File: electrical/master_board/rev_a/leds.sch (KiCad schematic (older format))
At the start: 50 parts, among them Q10 2N7000;SOT23, Q11 2N7000;SOT23, Q12 2N7000;SOT23, Q13 2N7000;SOT23, Q14 2N7000;SOT23, Q15 2N7000;SOT23, Q16 2N7000;SOT23, Q20 2N7000;SOT23, Q21 2N7000;SOT23, Q22 2N7000;SOT23, Q23 2N7000;SOT23, Q24 2N7000;SOT23, Q25 2N7000;SOT23, Q7 2N7000;SOT23, Q8 2N7000;SOT23, Q9 2N7000;SOT23, U5 SN74HCS595;TTSOP16, U8 SN74HCS595;TTSOP16

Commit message: Cleaned up schematics some.
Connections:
- net labels added: LED8_TO_LED9, LED_SCK, ~LED_NSS, ~NRST
- wire segments 187 -> 183
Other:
- moved on the sheet: U5, U8

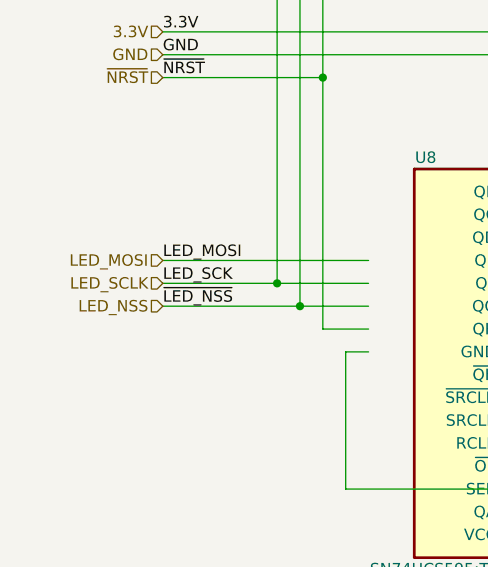
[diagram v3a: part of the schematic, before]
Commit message: Bound signals to Morpho pins.
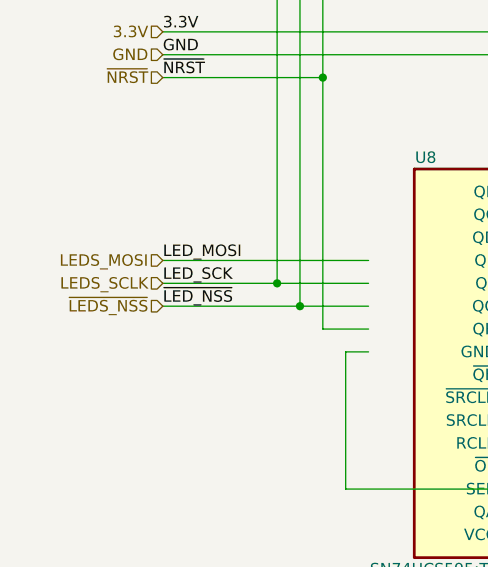
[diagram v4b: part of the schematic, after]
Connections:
- net labels added: LEDS_MOSI, LEDS_SCLK, ~LEDS_NSS
- net labels removed: LED_NSS, LED_SCLK
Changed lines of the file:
@@
 $Descr A4 11693 8268
 encoding utf-8
-Sheet 4 10
+Sheet 10 10
 Title "HR2 LED's"
 Date "2020-10-17"
@@
 	9700 3200 9700 2300
 Text HLabel 1000 5400 0    50   Input ~ 0
-LED_MOSI
+LEDS_MOSI
 Text HLabel 1000 5500 0    50   Input ~ 0
-LED_SCLK
+LEDS_SCLK
 $Comp
 L HR2:SN74HCS595;TTSOP16 U?
@@
 	3000 2700 6500 2700
 Text HLabel 1000 5600 0    50   Input ~ 0
-LED_NSS
+~LEDS_NSS
 Wire Bus Line
 	3500 2000 3500 6100

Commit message: Schematic is basically complete.
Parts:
- added C24, C25: 10pF;1608, symbol Device:C
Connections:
- wire segments 183 -> 189
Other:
- note added: "ByPass Capacitors"
- note added: "Power\nBus"
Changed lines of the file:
@@
 $Descr A4 11693 8268
 encoding utf-8
-Sheet 10 10
+Sheet 7 10
 Title "HR2 LED's"
 Date "2020-10-17"
@@
 Comment4 ""
 $EndDescr
-Text Notes 1050 1950 0    50   ~ 0
+Text Notes 900  1900 0    50   ~ 0
 Note:\n1. The LED's are controlled by a 16-bit shift regester that is\n   filled using an SPI controller.  The 3.3V outputs are fed into\n   FET's that drive the LED's.\n
-Connection ~ 4500 6400
-Wire Wire Line
-	4500 6400 3100 6400
 Wire Wire Line
 	9300 4200 10100 4200
@@
 AR Path="/5FA4A874/5FB58AAF" Ref="U8"  Part="1"
 F 0 "U8" H 2150 5250 50  0000 C CNN
-F 1 "SN74HCS595;TTSOP16" H 2300 3450 50  0000 C CNN
+F 1 "SN74HCS595;TTSOP16" H 2450 3950 50  0000 C CNN
 F 2 "Package_SO:TSSOP-16_4.4x5mm_P0.65mm" H 2100 5150 60  0001 L CNN
 F 3 "Tri-state 8-Bit Shift Register" H 2100 4950 60  0001 L CNN
@@
 Text Label 3400 5700 2    50   ~ 0
 LED6
-Text Notes 2250 1500 0    50   ~ 0
+Text Notes 1850 2000 0    50   ~ 0
 16-Bit SPI LED Shift Register
 Wire Wire Line
@@
 Text HLabel 1000 4500 0    50   Input ~ 0
 GND
-Wire Wire Line
-	10100 6400 10900 6400
-Wire Wire Line
-	10900 6400 10900 3500
-Wire Wire Line
-	10900 3500 10100 3500
-Connection ~ 10100 6400
-Connection ~ 10100 3500
-Wire Wire Line
-	4500 4200 3700 4200
-Wire Wire Line
-	3700 4200 3700 1300
-Wire Wire Line
-	3700 1300 4500 1300
 Connection ~ 4500 4200
 Text HLabel 1000 1300 0    50   Input ~ 0
@@
 Text HLabel 1000 4400 0    50   Input ~ 0
 3.3V
-Connection ~ 3700 1300
-Wire Wire Line
-	1000 1300 3700 1300
 Wire Wire Line
 	3000 5200 9700 5200
@@
 	3400 5100 3500 5000
 Entry Wire Line
-	3400 6100 3500 6000
+	3400 6400 3500 6300
 Wire Wire Line
 	3000 5100 3400 5100
 Wire Wire Line
-	3400 6100 3100 6100
+	3400 6400 3100 6400
 Wire Wire Line
 	1900 5800 1800 5800
@@
 Wire Wire Line
 	3100 6400 3100 6100
-Connection ~ 3100 6100
 Wire Wire Line
 	3100 6100 3000 6100
-Connection ~ 3100 6400
 Wire Wire Line
 	1800 6400 3100 6400
@@
 Text Label 3400 5100 2    50   ~ 0
 3.3V
-Text Label 3400 6100 2    50   ~ 0
+Text Label 3400 6400 2    50   ~ 0
 GND
 NoConn ~ 3000 6000
@@
 Text HLabel 1000 5600 0    50   Input ~ 0
 ~LEDS_NSS
+Text Notes 3250 3950 0    50   ~ 0
+Power\nBus
+Entry Wire Line
+	3600 3500 3500 3400
+Text Label 3600 3500 0    50   ~ 0
+GND
+Wire Wire Line
+	3600 3500 4500 3500
+Connection ~ 4500 3500
+Connection ~ 3100 6400
+Entry Wire Line
+	3600 6400 3500 6300
+Wire Wire Line
+	3600 6400 4500 6400
+Connection ~ 4500 6400
+Text Label 3600 6400 0    50   ~ 0
+GND
+Entry Wire Line
+	3500 1400 3400 1300
+Entry Wire Line
+	3500 1400 3600 1300
+Entry Wire Line
+	3950 1000 4050 1100
+Wire Wire Line
+	1000 1300 3400 1300
+Text Label 3400 1300 2    50   ~ 0
+P5V
+Text Label 3600 1300 0    50   ~ 0
+P5V
+Entry Wire Line
+	3500 4300 3600 4200
+Text Label 3600 4200 0    50   ~ 0
+P5V
+Wire Wire Line
+	3600 4200 4500 4200
+Wire Wire Line
+	3600 1300 4500 1300
+Text Label 3600 6600 0    50   ~ 0
+3.3V
+Text Label 3600 7200 0    50   ~ 0
+GND
+$Comp
+L Device:C C?
+U 1 1 5FA78555
+P 3800 6950
+AR Path="/5F48CAAD/5FA78555" Ref="C?"  Part="1"
+AR Path="/5F4CEE66/5FA78555" Ref="C?"  Part="1"
+AR Path="/5FA4A874/5FA78555" Ref="C24"  Part="1"
+F 0 "C24" H 3600 7050 50  0000 L CNN
+F 1 "10pF;1608" H 3850 6850 50  0000 L CNN
+F 2 "" H 3838 6800 50  0001 C CNN
+F 3 "~" H 3800 6950 50  0001 C CNN
+	1    3800 6950
+	1    0    0    -1
+$EndComp
+Wire Wire Line
+	3800 6800 3800 6700
+Wire Wire Line
+	3800 6700 3600 6700
+Wire Wire Line
+	3800 7100 3800 7200
+Entry Wire Line
+	3600 6600 3500 6500
+Entry Wire Line
+	3600 7200 3500 7100
+$Comp
+L Device:C C?
+U 1 1 5FA78560
+P 4400 6950
+AR Path="/5F48CAAD/5FA78560" Ref="C?"  Part="1"
+AR Path="/5F4CEE66/5FA78560" Ref="C?"  Part="1"
+AR Path="/5FA4A874/5FA78560" Ref="C25"  Part="1"
+F 0 "C25" H 4200 7050 50  0000 L CNN
+F 1 "10pF;1608" H 4450 6850 50  0000 L CNN
+F 2 "" H 4438 6800 50  0001 C CNN
+F 3 "~" H 4400 6950 50  0001 C CNN
+	1    4400 6950
+	1    0    0    -1
+$EndComp
+Wire Wire Line
+	3800 6700 4400 6700
+Connection ~ 3800 6700
+Wire Wire Line
+	4400 6800 4400 6700
+Wire Wire Line
+	3800 7200 4400 7200
+Wire Wire Line
+	4400 7100 4400 7200
+Wire Wire Line
+	3600 6700 3600 6600
+Text Notes 3800 6650 0    50   ~ 0
+ByPass Capacitors
+Wire Wire Line
+	3600 7200 3800 7200
 Wire Bus Line
-	3500 2000 3500 6100
+	3500 1300 3500 7200
+Connection ~ 3800 7200
 $EndSCHEMATC

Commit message: Reannoted. Postioned components are in the 80-99 reference range.
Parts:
- renumbered C24 to C20, C25 to C21, D23 to D81, D21 to D82, D19 to D83, D14 to D84, D12 to D85, D10 to D86, D8 to D87, D6 to D88, D22 to D89, D20 to D90, D18 to D91, D13 to D92, D11 to D93, D9 to D94, D7 to D95, D5 to D96, Q13 to Q10, Q14 to Q11, Q15 to Q12, Q16 to Q13, Q20 to Q14, Q21 to Q15, Q22 to Q16, Q23 to Q17, Q24 to Q18, Q25 to Q19, Q7 to Q4, Q8 to Q5, Q9 to Q6, Q10 to Q7, Q11 to Q8, Q12 to Q9, R23 to R37, R24 to R38, R25 to R39, R26 to R40, R27 to R41, R28 to R42, R29 to R43, R30 to R44, R31 to R45, R32 to R46, R33 to R47, R34 to R48, R44 to R49, R45 to R50, R46 to R51, R47 to R52, U5 to U11, U8 to U12
